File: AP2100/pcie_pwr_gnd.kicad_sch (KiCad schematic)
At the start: 80 parts

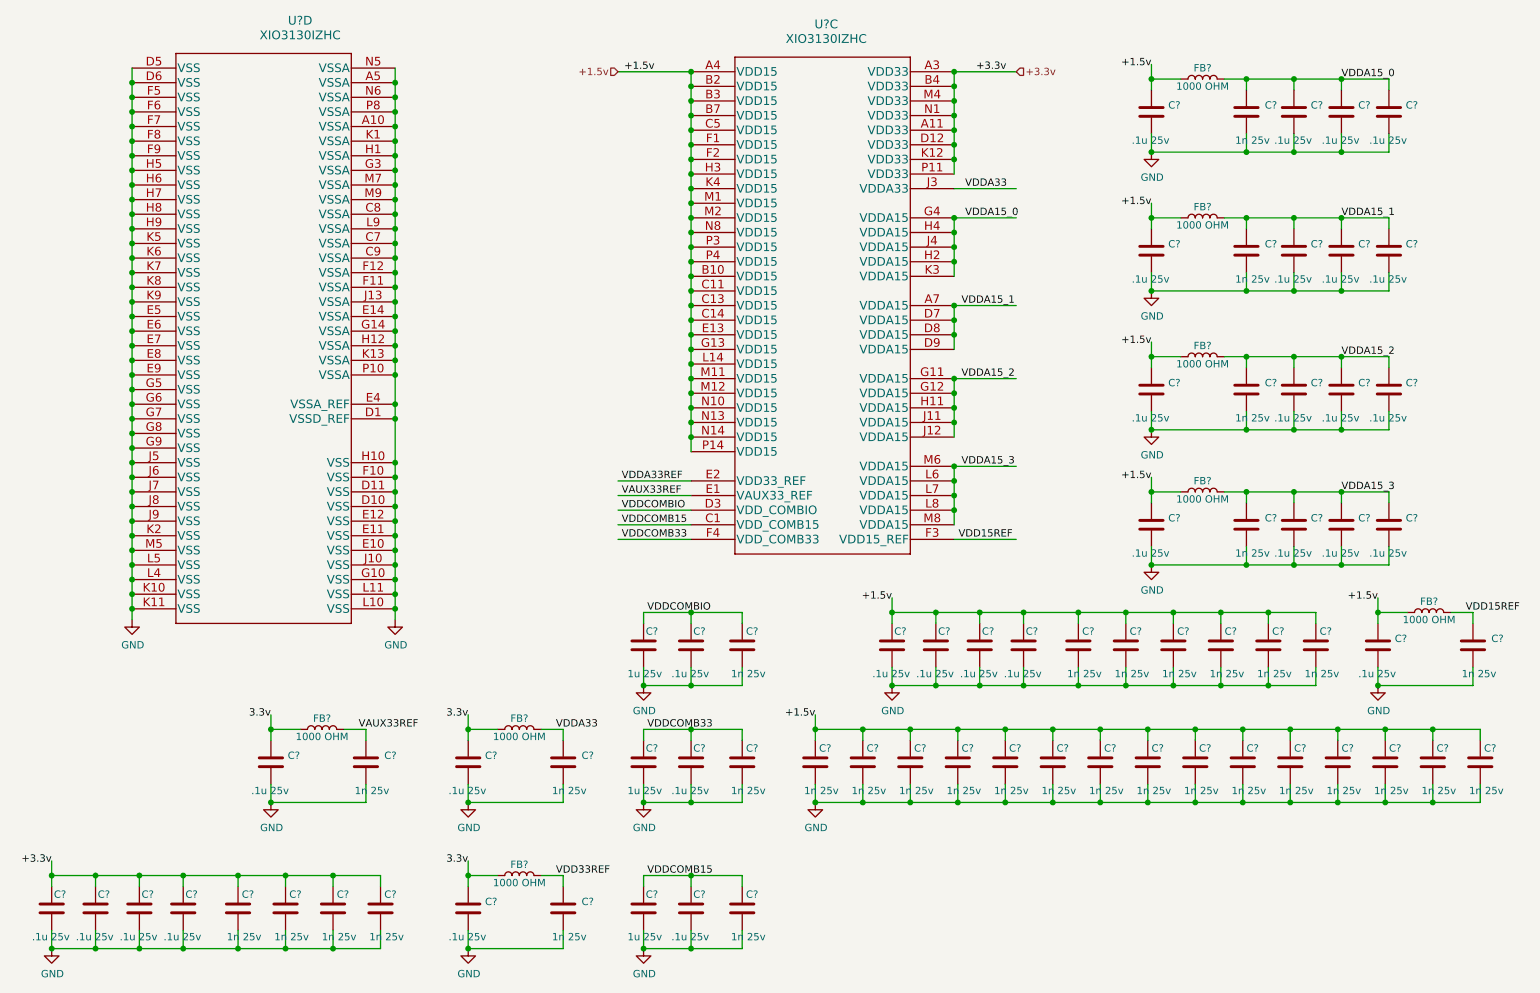
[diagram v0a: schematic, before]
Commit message: Add AP3000 single radio for security cameras. Add CM4IO Raspi board
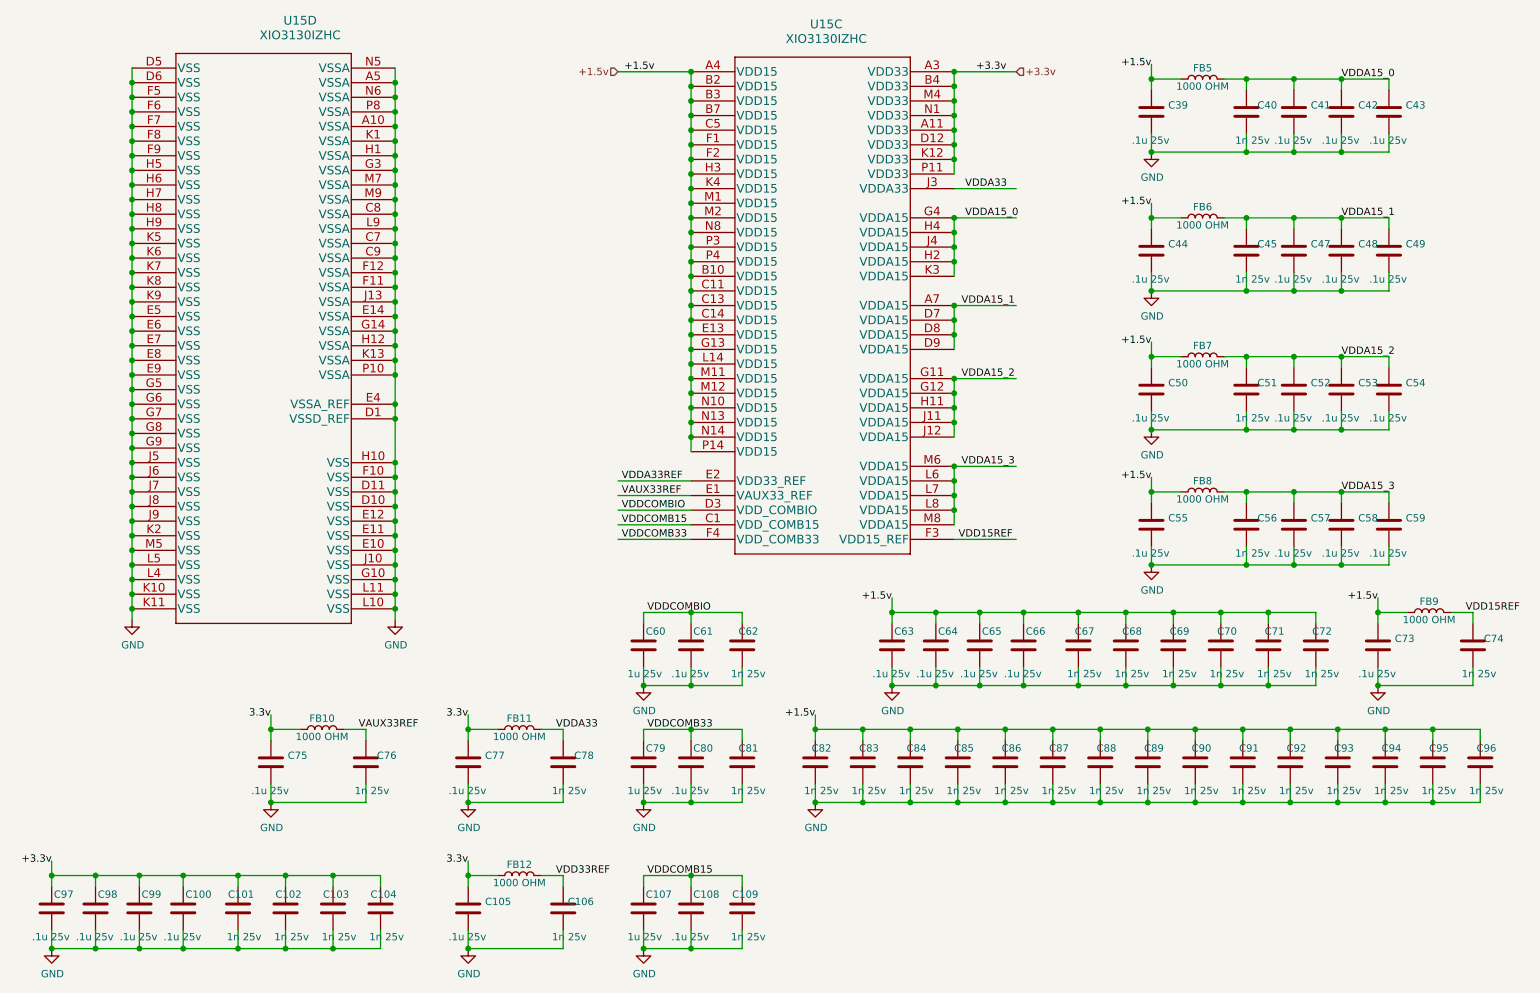
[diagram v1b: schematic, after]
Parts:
- gave numbers to parts that had none: 79
